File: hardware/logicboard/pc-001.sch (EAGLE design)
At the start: 17 parts, among them J4 DNP, J5 DNP

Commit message: Flipped I2C connector.
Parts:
- renumbered ANALOG to ANALOG-PULLDOWN
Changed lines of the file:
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@@
 <part name="SUPPLY2" library="supply2" library_urn="urn:adsk.eagle:library:372" deviceset="GND" device=""/>
 <part name="C1" library="resistor" library_urn="urn:adsk.eagle:library:348" deviceset="C-US" device="025-025X050" package3d_urn="urn:adsk.eagle:package:26151/1" value="0.1u"/>
-<part name="ANALOG" library="con-ml" library_urn="urn:adsk.eagle:library:164" deviceset="ML14L" device="" package3d_urn="urn:adsk.eagle:package:8677/1"/>
+<part name="ANALOG-PULLDOWN" library="con-ml" library_urn="urn:adsk.eagle:library:164" deviceset="ML14L" device="" package3d_urn="urn:adsk.eagle:package:8677/1"/>
 <part name="L1" library="SparkFun-Connectors" library_urn="urn:adsk.eagle:library:513" deviceset="CONN_02" device="-JST-2-PTH-NO_SILK" package3d_urn="urn:adsk.eagle:package:38056/1"/>
 <part name="L2" library="SparkFun-Connectors" library_urn="urn:adsk.eagle:library:513" deviceset="CONN_02" device="-JST-2-PTH-NO_SILK" package3d_urn="urn:adsk.eagle:package:38056/1"/>
@@
 <part name="R4" library="resistor" library_urn="urn:adsk.eagle:library:348" deviceset="R-EU_" device="0204/5" package3d_urn="urn:adsk.eagle:package:25955/1" value="6.8k"/>
 <part name="MMA8452Q" library="SparkFun-Connectors" library_urn="urn:adsk.eagle:library:513" deviceset="CONN_06" device="NO_SILK_FEMALE_PTH" package3d_urn="urn:adsk.eagle:package:38130/1"/>
-<part name="FRAME2" library="frames" library_urn="urn:adsk.eagle:library:229" deviceset="A4L-LOC" device=""/>
+<part name="FRAME" library="frames" library_urn="urn:adsk.eagle:library:229" deviceset="A4L-LOC" device=""/>
 <part name="LOGO1" library="SparkFun-Aesthetics" deviceset="OSHW-LOGO" device="S-COPPER" value="OSHW-LOGOS-COPPER"/>
 <part name="U$1" library="pineapple" deviceset="PINEAPPLE450" device=""/>
@@
 <instance part="SUPPLY2" gate="GND" x="48.26" y="48.26"/>
 <instance part="C1" gate="G$1" x="134.62" y="99.06"/>
-<instance part="ANALOG" gate="1" x="93.98" y="127" rot="MR180"/>
+<instance part="ANALOG-PULLDOWN" gate="1" x="93.98" y="127" rot="MR180"/>
 <instance part="L1" gate="G$1" x="157.48" y="88.9" rot="R180"/>
 <instance part="L2" gate="G$1" x="157.48" y="73.66" rot="R180"/>
@@
 <instance part="R4" gate="G$1" x="175.26" y="96.52" rot="R90"/>
 <instance part="MMA8452Q" gate="G$1" x="187.96" y="86.36" rot="R180"/>
-<instance part="FRAME2" gate="G$1" x="0" y="0"/>
+<instance part="FRAME" gate="G$1" x="0" y="0"/>
 <instance part="LOGO1" gate="G$1" x="241.3" y="165.1"/>
 <instance part="U$1" gate="G$1" x="187.96" y="7.62"/>
@@
 <wire x1="55.88" y1="134.62" x2="55.88" y2="106.68" width="0.1524" layer="91"/>
 <junction x="55.88" y="106.68"/>
-<pinref part="ANALOG" gate="1" pin="2"/>
+<pinref part="ANALOG-PULLDOWN" gate="1" pin="2"/>
 <wire x1="55.88" y1="134.62" x2="86.36" y2="134.62" width="0.1524" layer="91"/>
 <label x="86.36" y="106.68" size="1.778" layer="95"/>
@@
 <wire x1="58.42" y1="132.08" x2="58.42" y2="104.14" width="0.1524" layer="91"/>
 <junction x="58.42" y="104.14"/>
-<pinref part="ANALOG" gate="1" pin="4"/>
+<pinref part="ANALOG-PULLDOWN" gate="1" pin="4"/>
 <wire x1="58.42" y1="132.08" x2="86.36" y2="132.08" width="0.1524" layer="91"/>
 <label x="86.36" y="104.14" size="1.778" layer="95"/>
@@
 <wire x1="134.62" y1="101.6" x2="134.62" y2="104.14" width="0.1524" layer="91"/>
 <junction x="134.62" y="104.14"/>
-<pinref part="ANALOG" gate="1" pin="1"/>
+<pinref part="ANALOG-PULLDOWN" gate="1" pin="1"/>
 <wire x1="104.14" y1="134.62" x2="101.6" y2="134.62" width="0.1524" layer="91"/>
-<pinref part="ANALOG" gate="1" pin="3"/>
+<pinref part="ANALOG-PULLDOWN" gate="1" pin="3"/>
 <wire x1="101.6" y1="132.08" x2="104.14" y2="132.08" width="0.1524" layer="91"/>
 <junction x="104.14" y="132.08"/>
-<pinref part="ANALOG" gate="1" pin="5"/>
+<pinref part="ANALOG-PULLDOWN" gate="1" pin="5"/>
 <wire x1="101.6" y1="129.54" x2="104.14" y2="129.54" width="0.1524" layer="91"/>
 <junction x="104.14" y="129.54"/>
-<pinref part="ANALOG" gate="1" pin="7"/>
+<pinref part="ANALOG-PULLDOWN" gate="1" pin="7"/>
 <wire x1="101.6" y1="127" x2="104.14" y2="127" width="0.1524" layer="91"/>
 <junction x="104.14" y="127"/>
-<pinref part="ANALOG" gate="1" pin="9"/>
+<pinref part="ANALOG-PULLDOWN" gate="1" pin="9"/>
 <wire x1="101.6" y1="124.46" x2="104.14" y2="124.46" width="0.1524" layer="91"/>
 <junction x="104.14" y="124.46"/>
-<pinref part="ANALOG" gate="1" pin="11"/>
+<pinref part="ANALOG-PULLDOWN" gate="1" pin="11"/>
 <wire x1="101.6" y1="121.92" x2="104.14" y2="121.92" width="0.1524" layer="91"/>
 <junction x="104.14" y="121.92"/>
-<pinref part="ANALOG" gate="1" pin="13"/>
+<pinref part="ANALOG-PULLDOWN" gate="1" pin="13"/>
 <wire x1="101.6" y1="119.38" x2="104.14" y2="119.38" width="0.1524" layer="91"/>
 <junction x="104.14" y="119.38"/>
@@
 <wire x1="60.96" y1="129.54" x2="60.96" y2="101.6" width="0.1524" layer="91"/>
 <junction x="60.96" y="101.6"/>
-<pinref part="ANALOG" gate="1" pin="6"/>
+<pinref part="ANALOG-PULLDOWN" gate="1" pin="6"/>
 <wire x1="60.96" y1="129.54" x2="86.36" y2="129.54" width="0.1524" layer="91"/>
 <label x="86.36" y="101.6" size="1.778" layer="95"/>
@@
 <wire x1="63.5" y1="127" x2="63.5" y2="99.06" width="0.1524" layer="91"/>
 <junction x="63.5" y="99.06"/>
-<pinref part="ANALOG" gate="1" pin="8"/>
+<pinref part="ANALOG-PULLDOWN" gate="1" pin="8"/>
 <wire x1="63.5" y1="127" x2="86.36" y2="127" width="0.1524" layer="91"/>
 <label x="86.36" y="99.06" size="1.778" layer="95"/>
@@
 <wire x1="66.04" y1="124.46" x2="66.04" y2="96.52" width="0.1524" layer="91"/>
 <junction x="66.04" y="96.52"/>
-<pinref part="ANALOG" gate="1" pin="10"/>
+<pinref part="ANALOG-PULLDOWN" gate="1" pin="10"/>
 <wire x1="66.04" y1="124.46" x2="86.36" y2="124.46" width="0.1524" layer="91"/>
 <label x="86.36" y="96.52" size="1.778" layer="95"/>
@@
 <wire x1="68.58" y1="121.92" x2="68.58" y2="93.98" width="0.1524" layer="91"/>
 <junction x="68.58" y="93.98"/>
-<pinref part="ANALOG" gate="1" pin="12"/>
+<pinref part="ANALOG-PULLDOWN" gate="1" pin="12"/>
 <wire x1="68.58" y1="121.92" x2="86.36" y2="121.92" width="0.1524" layer="91"/>
 <label x="86.36" y="93.98" size="1.778" layer="95"/>
@@
 <wire x1="71.12" y1="119.38" x2="71.12" y2="91.44" width="0.1524" layer="91"/>
 <junction x="71.12" y="91.44"/>
-<pinref part="ANALOG" gate="1" pin="14"/>
+<pinref part="ANALOG-PULLDOWN" gate="1" pin="14"/>
 <wire x1="71.12" y1="119.38" x2="86.36" y2="119.38" width="0.1524" layer="91"/>
 <label x="86.36" y="91.44" size="1.778" layer="95"/>

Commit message: Fixed error of version number on the schematic.
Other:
- note added: "PineappleCake 1.2.0 for MKR1000"
- note removed: "PineappleCake 2.0.0 for MKR1000"
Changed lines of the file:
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@@
 <sheet>
 <plain>
-<text x="215.9" y="20.32" size="1.778" layer="94">PineappleCake 2.0.0 for MKR1000</text>
+<text x="215.9" y="20.32" size="1.778" layer="94">PineappleCake 1.2.0 for MKR1000</text>
 </plain>
 <instances>

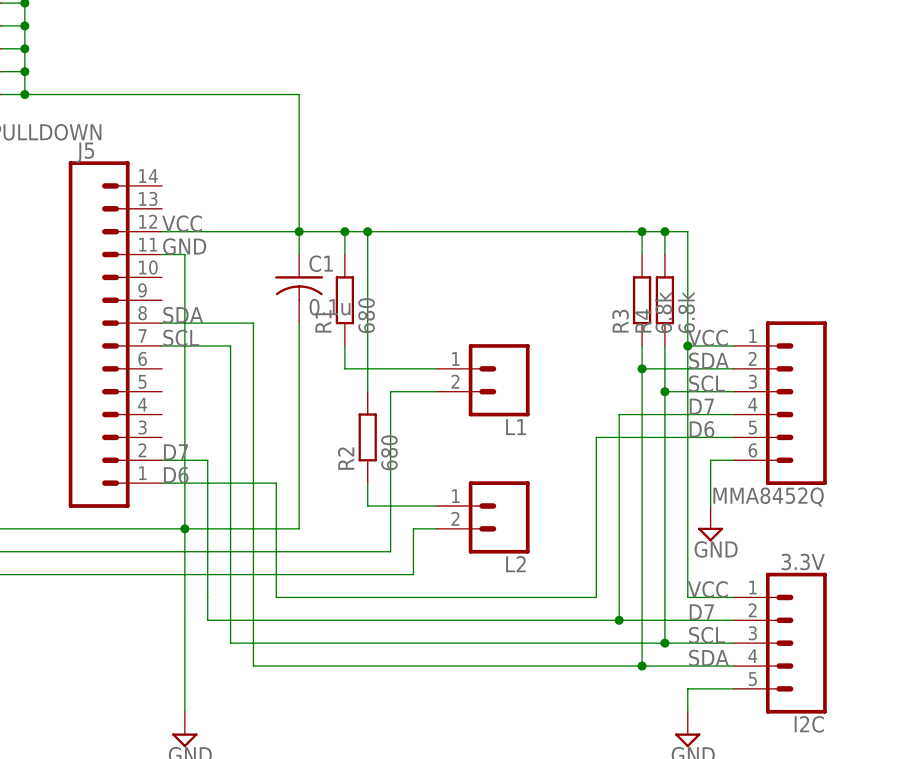
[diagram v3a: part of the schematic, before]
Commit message: 1st pin of I2C connector now has 5V supply, not 3.3V.
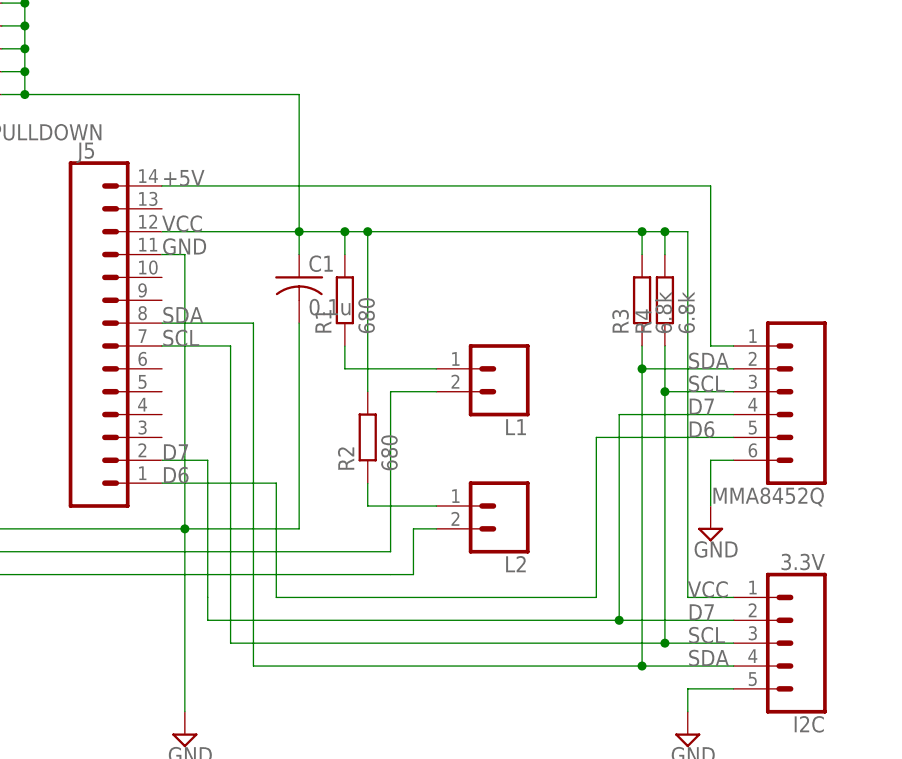
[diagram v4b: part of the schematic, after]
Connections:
- new net +5V: J5.14, MMA8452Q.1
- net VCC: no longer MMA8452Q.1
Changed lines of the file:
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@@
 <wire x1="172.72" y1="104.14" x2="175.26" y2="104.14" width="0.1524" layer="91"/>
 <wire x1="175.26" y1="104.14" x2="177.8" y2="104.14" width="0.1524" layer="91"/>
-<wire x1="177.8" y1="104.14" x2="177.8" y2="91.44" width="0.1524" layer="91"/>
-<wire x1="177.8" y1="91.44" x2="177.8" y2="63.5" width="0.1524" layer="91"/>
+<wire x1="177.8" y1="104.14" x2="177.8" y2="63.5" width="0.1524" layer="91"/>
 <wire x1="177.8" y1="63.5" x2="182.88" y2="63.5" width="0.1524" layer="91"/>
 <label x="177.8" y="63.5" size="1.778" layer="95"/>
@@
 <wire x1="175.26" y1="101.6" x2="175.26" y2="104.14" width="0.1524" layer="91"/>
 <junction x="175.26" y="104.14"/>
-<pinref part="MMA8452Q" gate="G$1" pin="1"/>
-<wire x1="182.88" y1="91.44" x2="177.8" y2="91.44" width="0.1524" layer="91"/>
-<junction x="177.8" y="91.44"/>
-<label x="177.8" y="91.44" size="1.778" layer="95"/>
 <label x="119.38" y="104.14" size="1.778" layer="95"/>
 </segment>
@@
 </segment>
 </net>
+<net name="+5V" class="2">
+<segment>
+<pinref part="J5" gate="G$1" pin="14"/>
+<wire x1="119.38" y1="109.22" x2="180.34" y2="109.22" width="0.1524" layer="91"/>
+<wire x1="180.34" y1="109.22" x2="180.34" y2="91.44" width="0.1524" layer="91"/>
+<pinref part="MMA8452Q" gate="G$1" pin="1"/>
+<wire x1="180.34" y1="91.44" x2="182.88" y2="91.44" width="0.1524" layer="91"/>
+<label x="119.38" y="109.22" size="1.778" layer="95"/>
+</segment>
+</net>

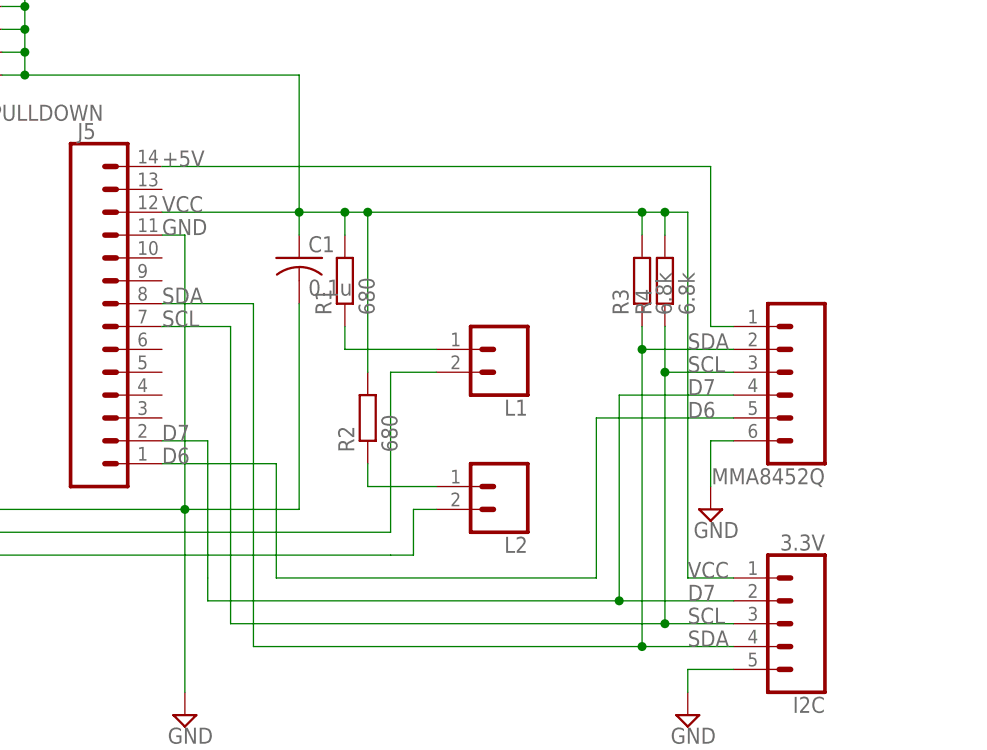
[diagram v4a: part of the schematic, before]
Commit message: Hotfix. I2C connector is now connected to +5V, not +3.3V (Vcc).
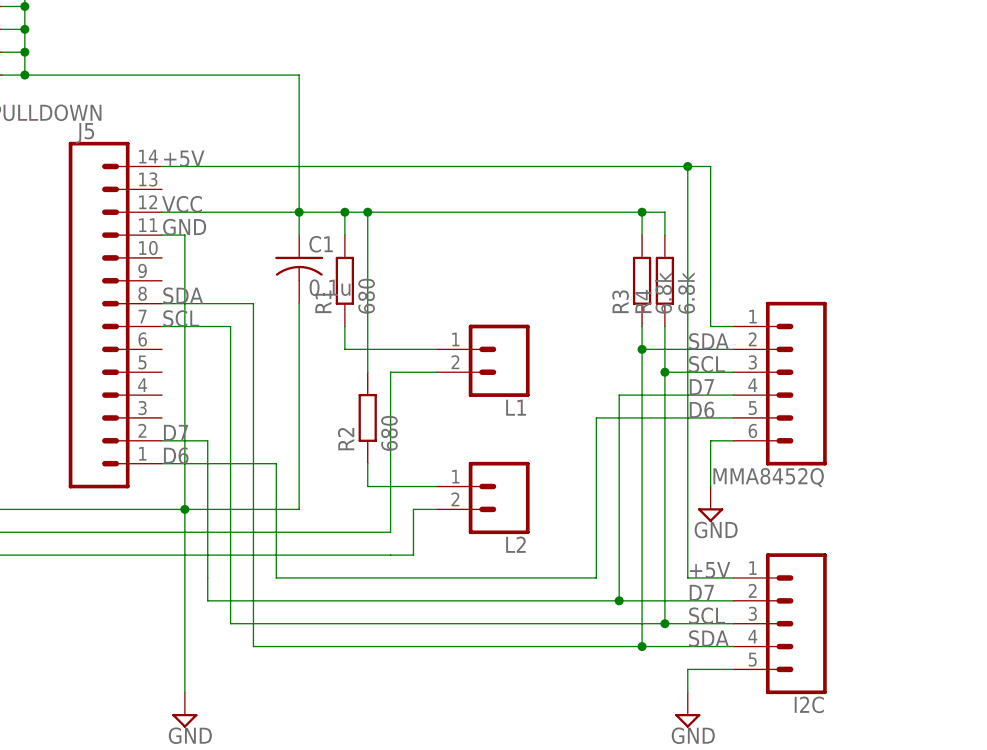
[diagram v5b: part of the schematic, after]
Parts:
- I2C: value 3.3V -> (none)
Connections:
- net +5V: now also I2C.1
- net VCC: no longer I2C.1
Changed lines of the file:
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@@
 <part name="L1" library="SparkFun-Connectors" library_urn="urn:adsk.eagle:library:513" deviceset="CONN_02" device="-JST-2-PTH-NO_SILK" package3d_urn="urn:adsk.eagle:package:38056/1"/>
 <part name="L2" library="SparkFun-Connectors" library_urn="urn:adsk.eagle:library:513" deviceset="CONN_02" device="-JST-2-PTH-NO_SILK" package3d_urn="urn:adsk.eagle:package:38056/1"/>
-<part name="I2C" library="SparkFun-Connectors" library_urn="urn:adsk.eagle:library:513" deviceset="CONN_05" device="SMD" package3d_urn="urn:adsk.eagle:package:38026/1" value="3.3V"/>
+<part name="I2C" library="SparkFun-Connectors" library_urn="urn:adsk.eagle:library:513" deviceset="CONN_05" device="SMD" package3d_urn="urn:adsk.eagle:package:38026/1"/>
 <part name="SUPPLY3" library="supply2" library_urn="urn:adsk.eagle:library:372" deviceset="GND" device=""/>
 <part name="SUPPLY4" library="supply2" library_urn="urn:adsk.eagle:library:372" deviceset="GND" device=""/>
@@
 <junction x="104.14" y="119.38"/>
 <wire x1="134.62" y1="104.14" x2="139.7" y2="104.14" width="0.1524" layer="91"/>
-<pinref part="I2C" gate="G$1" pin="1"/>
 <wire x1="139.7" y1="104.14" x2="142.24" y2="104.14" width="0.1524" layer="91"/>
 <wire x1="142.24" y1="104.14" x2="172.72" y2="104.14" width="0.1524" layer="91"/>
 <wire x1="172.72" y1="104.14" x2="175.26" y2="104.14" width="0.1524" layer="91"/>
-<wire x1="175.26" y1="104.14" x2="177.8" y2="104.14" width="0.1524" layer="91"/>
-<wire x1="177.8" y1="104.14" x2="177.8" y2="63.5" width="0.1524" layer="91"/>
-<wire x1="177.8" y1="63.5" x2="182.88" y2="63.5" width="0.1524" layer="91"/>
-<label x="177.8" y="63.5" size="1.778" layer="95"/>
 <pinref part="R1" gate="G$1" pin="2"/>
 <wire x1="139.7" y1="104.14" x2="139.7" y2="101.6" width="0.1524" layer="91"/>
@@
 <pinref part="R4" gate="G$1" pin="2"/>
 <wire x1="175.26" y1="101.6" x2="175.26" y2="104.14" width="0.1524" layer="91"/>
-<junction x="175.26" y="104.14"/>
 <label x="119.38" y="104.14" size="1.778" layer="95"/>
 </segment>
@@
 <segment>
 <pinref part="J5" gate="G$1" pin="14"/>
-<wire x1="119.38" y1="109.22" x2="180.34" y2="109.22" width="0.1524" layer="91"/>
+<wire x1="119.38" y1="109.22" x2="177.8" y2="109.22" width="0.1524" layer="91"/>
+<wire x1="177.8" y1="109.22" x2="180.34" y2="109.22" width="0.1524" layer="91"/>
 <wire x1="180.34" y1="109.22" x2="180.34" y2="91.44" width="0.1524" layer="91"/>
 <pinref part="MMA8452Q" gate="G$1" pin="1"/>
 <wire x1="180.34" y1="91.44" x2="182.88" y2="91.44" width="0.1524" layer="91"/>
 <label x="119.38" y="109.22" size="1.778" layer="95"/>
-</segment>
-</net>
+<pinref part="I2C" gate="G$1" pin="1"/>
+<wire x1="177.8" y1="63.5" x2="182.88" y2="63.5" width="0.1524" layer="91"/>
+<label x="177.8" y="63.5" size="1.778" layer="95"/>
+<wire x1="177.8" y1="63.5" x2="177.8" y2="109.22" width="0.1524" layer="91"/>
+<junction x="177.8" y="109.22"/>
+</segment>
+</net>

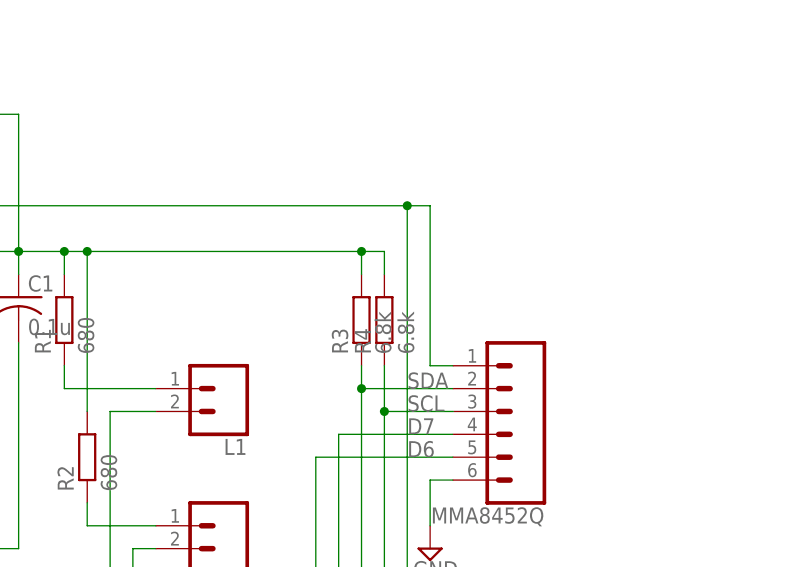
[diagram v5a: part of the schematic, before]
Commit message: Fixed wrong connection to MMA8452Q.
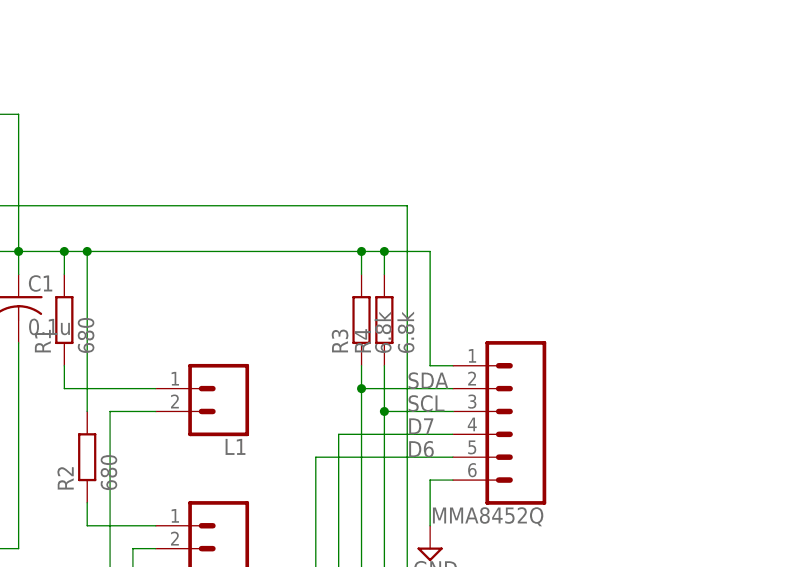
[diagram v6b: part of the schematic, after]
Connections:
- net +5V: no longer MMA8452Q.1
- net VCC: now also MMA8452Q.1
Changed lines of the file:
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@@
 <wire x1="175.26" y1="101.6" x2="175.26" y2="104.14" width="0.1524" layer="91"/>
 <label x="119.38" y="104.14" size="1.778" layer="95"/>
+<pinref part="MMA8452Q" gate="G$1" pin="1"/>
+<wire x1="180.34" y1="91.44" x2="182.88" y2="91.44" width="0.1524" layer="91"/>
+<wire x1="175.26" y1="104.14" x2="180.34" y2="104.14" width="0.1524" layer="91"/>
+<wire x1="180.34" y1="104.14" x2="180.34" y2="91.44" width="0.1524" layer="91"/>
+<junction x="175.26" y="104.14"/>
 </segment>
 </net>
@@
 <pinref part="J5" gate="G$1" pin="14"/>
 <wire x1="119.38" y1="109.22" x2="177.8" y2="109.22" width="0.1524" layer="91"/>
-<wire x1="177.8" y1="109.22" x2="180.34" y2="109.22" width="0.1524" layer="91"/>
-<wire x1="180.34" y1="109.22" x2="180.34" y2="91.44" width="0.1524" layer="91"/>
-<pinref part="MMA8452Q" gate="G$1" pin="1"/>
-<wire x1="180.34" y1="91.44" x2="182.88" y2="91.44" width="0.1524" layer="91"/>
 <label x="119.38" y="109.22" size="1.778" layer="95"/>
 <pinref part="I2C" gate="G$1" pin="1"/>
@@
 <label x="177.8" y="63.5" size="1.778" layer="95"/>
 <wire x1="177.8" y1="63.5" x2="177.8" y2="109.22" width="0.1524" layer="91"/>
-<junction x="177.8" y="109.22"/>
-</segment>
-</net>
+</segment>
+</net>
